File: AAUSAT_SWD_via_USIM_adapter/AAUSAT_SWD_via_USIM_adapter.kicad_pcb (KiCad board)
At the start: 2 copper layers, 55.2 x 22 mm, 6 parts, among them J1 SIM_Card, J2 AAUSAT_JTAG

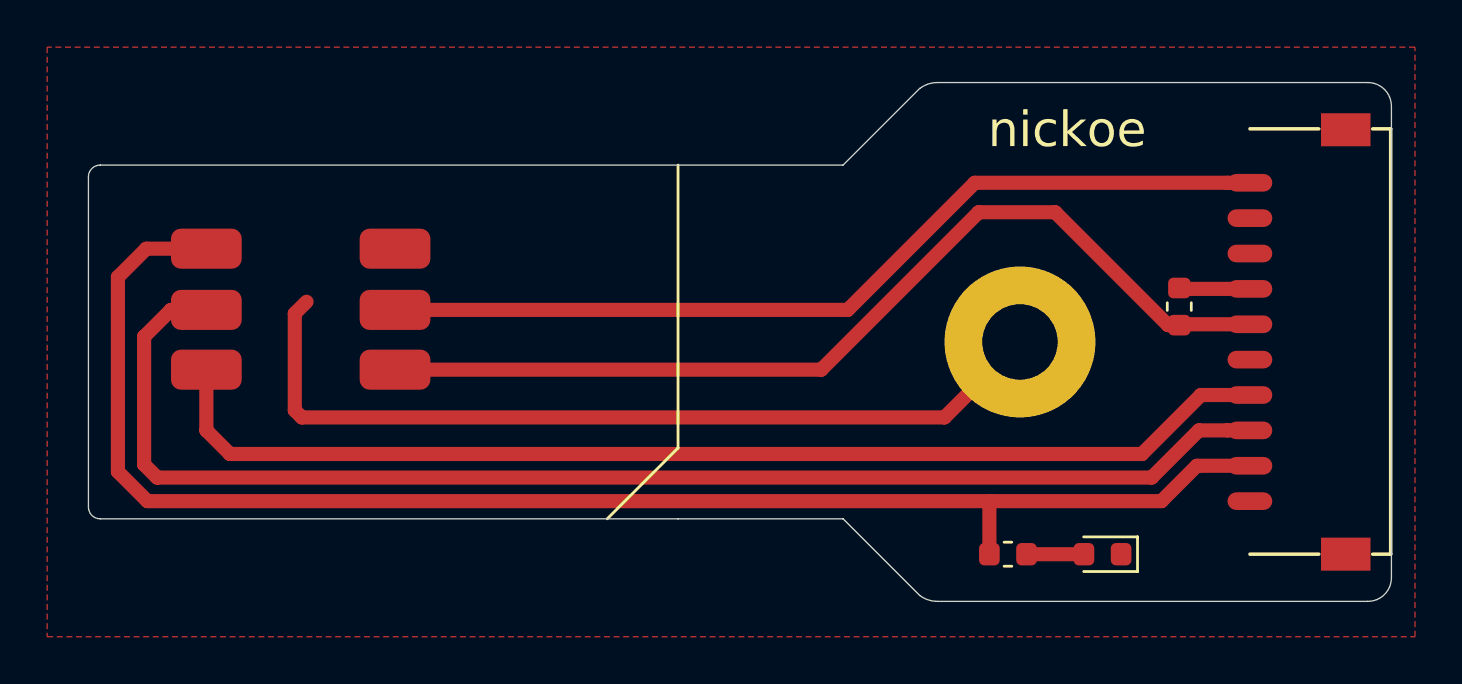
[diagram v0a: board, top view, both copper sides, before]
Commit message: Shorten adapter, it was a bit too long
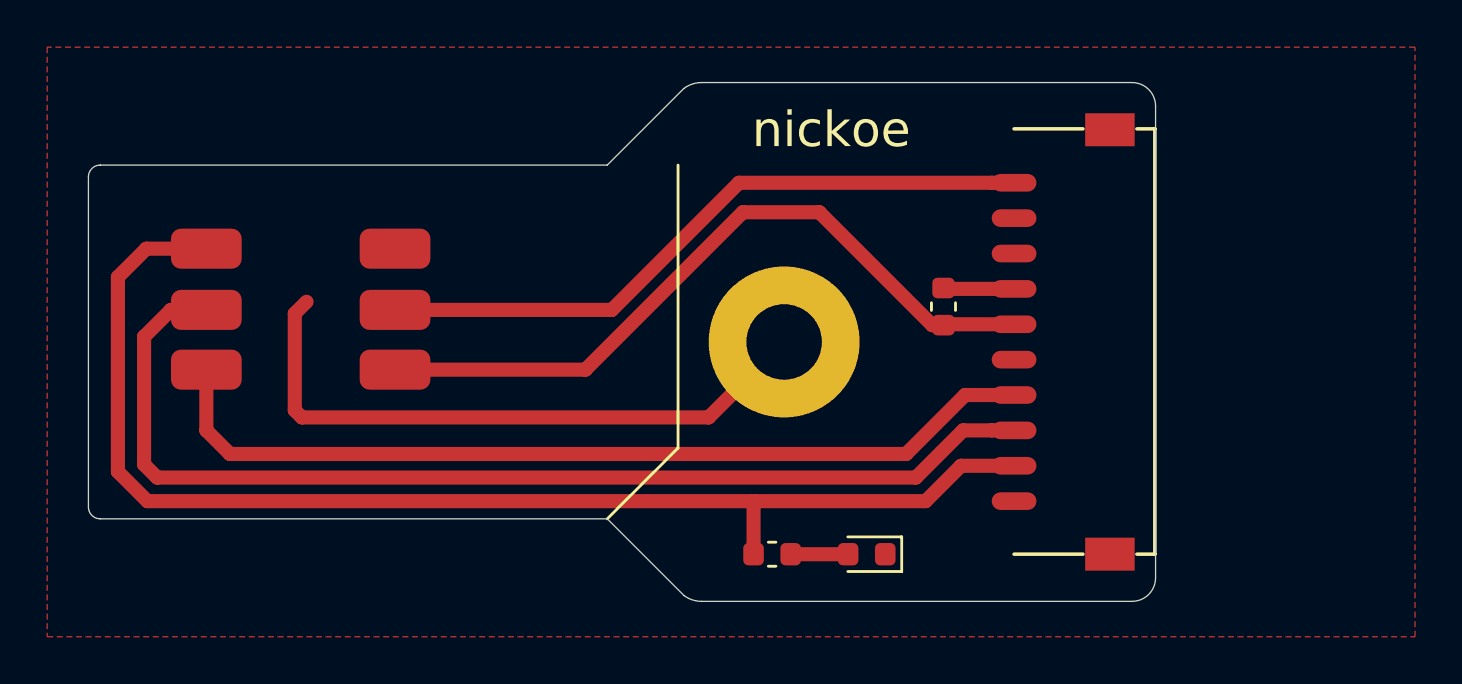
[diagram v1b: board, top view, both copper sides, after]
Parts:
- moved D1 10.0 mm to (154.8, 74.5)
- moved H1 10.0 mm to (151.2, 65.5)
- moved J2 10.0 mm to (161.0, 58.8)
- moved R1 10.0 mm to (158.0, 64.0)
- moved R2 10.0 mm to (150.7, 74.5)
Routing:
- net GND: track 37.0 -> 27.0 mm
- net /SWCLK: track 48.3 -> 38.3 mm
- net /STM_RESET: track 56.5 -> 46.5 mm
- net +3V3: track 63.9 -> 53.9 mm
- net /UART4_TX: track 38.5 -> 28.5 mm
- net /SWDIO: track 41.0 -> 31.0 mm
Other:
- board size 55.2 x 22 mm -> 45.2 x 22 mm

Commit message: Add skunk and name of board
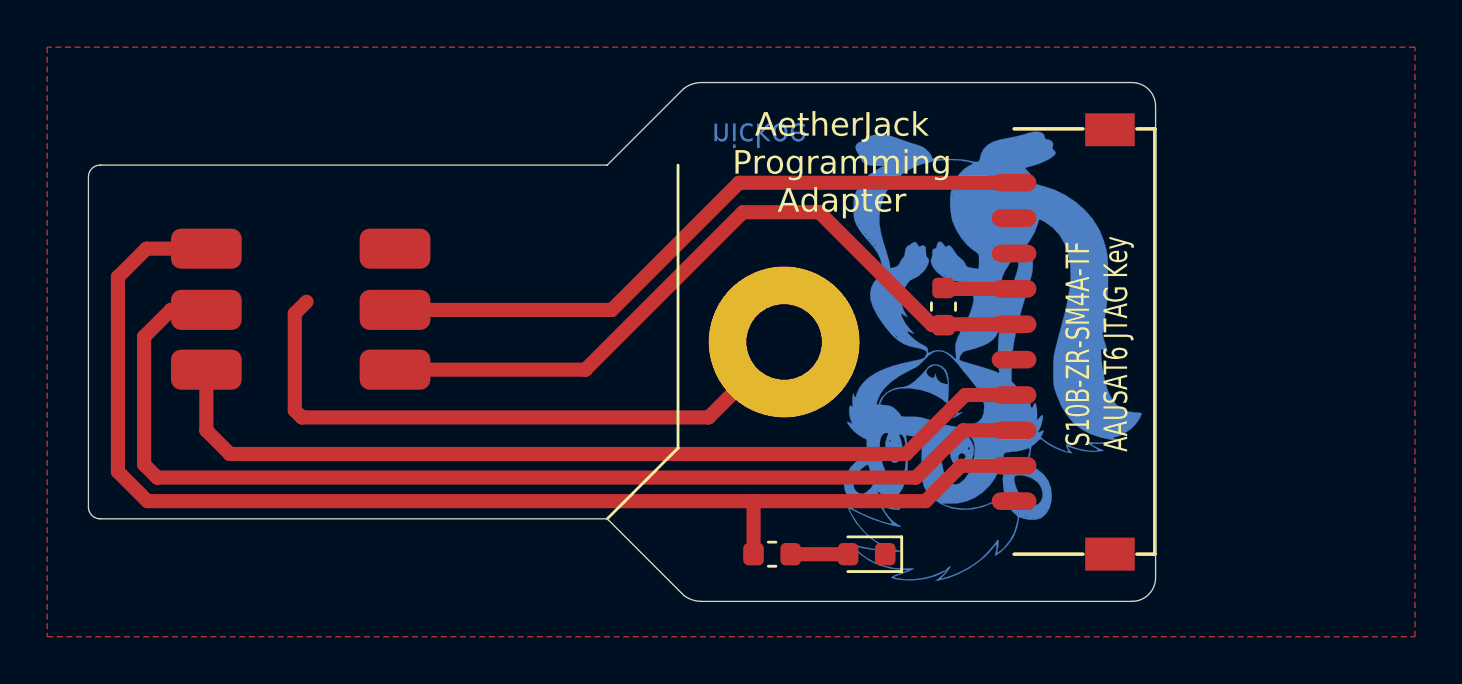
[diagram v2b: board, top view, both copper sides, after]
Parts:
- added G***: LOGO, aausat:skunk, B.Cu at (160.1, 66.1)
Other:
- board text added: "AetherJack Programming Adapter"
- board text added: "S10B-ZR-SM4A-TF AAUSAT6 JTAG Key"

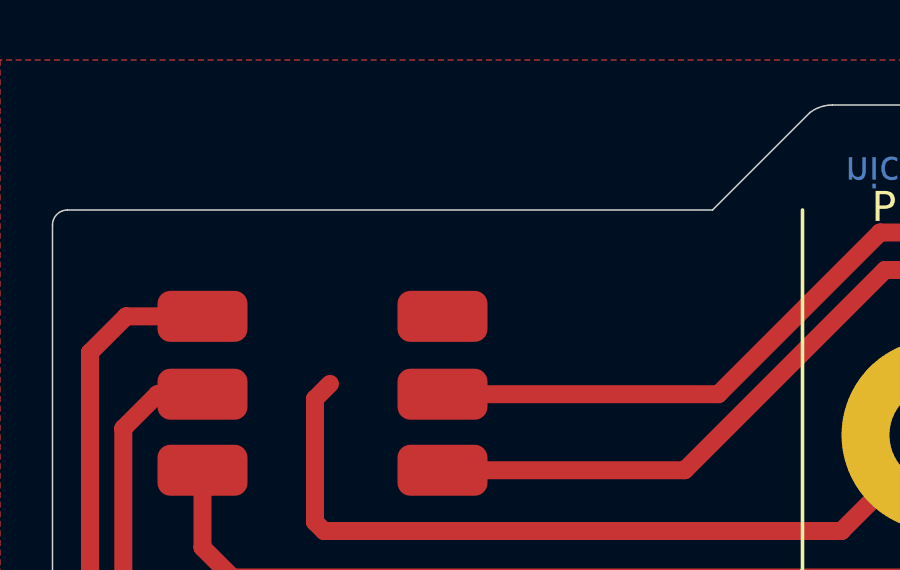
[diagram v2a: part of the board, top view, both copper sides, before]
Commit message: Add date on adapter
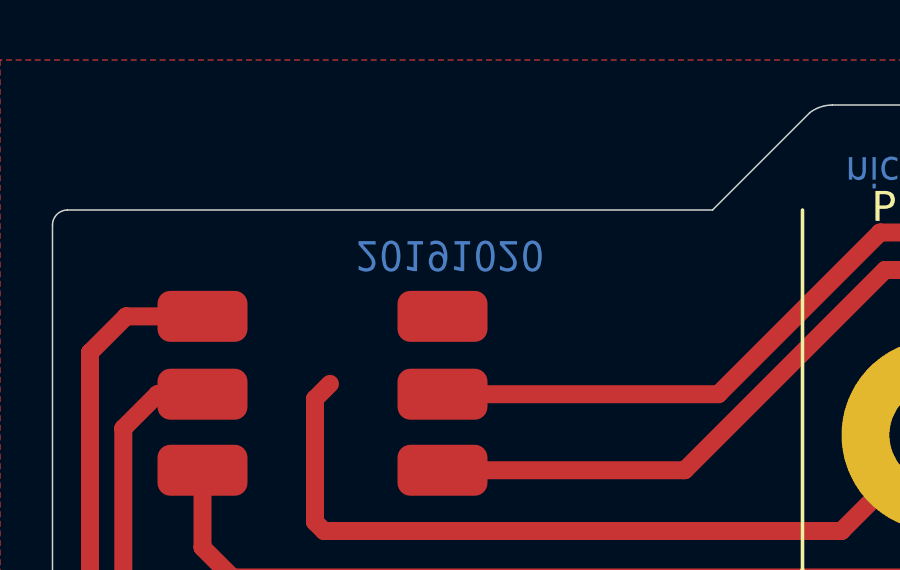
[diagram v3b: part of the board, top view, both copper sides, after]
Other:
- board text added: "20191020"
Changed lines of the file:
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@@
   (general
     (thickness 0.8)
-    (drawings 19)
+    (drawings 20)
     (tracks 43)
     (zones 0)
@@
     )
   )
+  (gr_text 20191020 (at 135 59.5 180) (layer B.Cu)
+    (effects (font (size 1 0.9) (thickness 0.15)) (justify mirror))
+  )
   (gr_text "AetherJack\nProgramming\nAdapter" (at 153.7 57.9) (layer F.SilkS)
